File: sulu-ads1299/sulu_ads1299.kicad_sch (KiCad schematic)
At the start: 27 parts, among them J1 Conn_02x11_Odd_Even, J2 Conn_02x10_Odd_Even, J3 Conn_01x10, J4 Conn_02x07_Odd_Even, J5 73391-0060, J6 Conn_01x02, SW1 SW_Push, U3 S-85S1AB18-I6T1U, U4 S-85S1AB11-I6T1U, U5 LM2775DSG

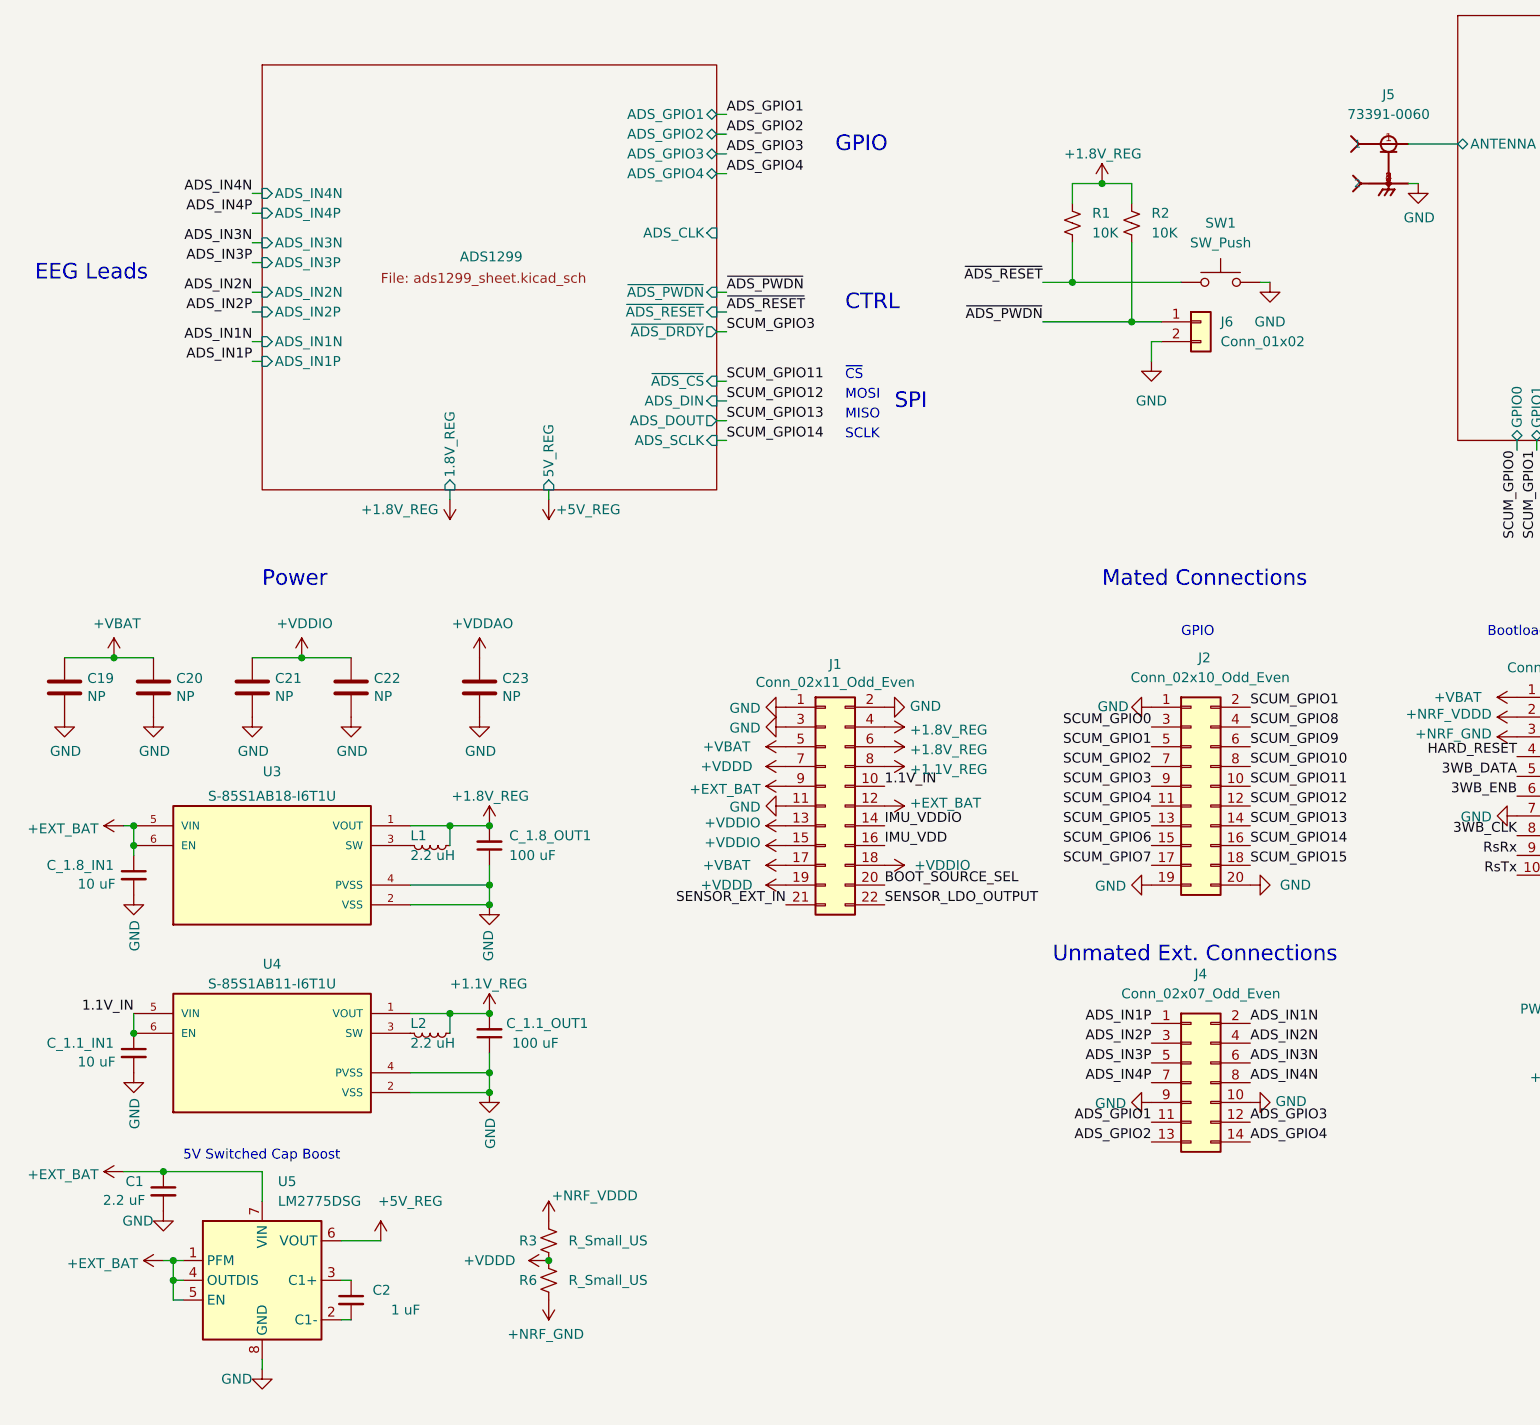
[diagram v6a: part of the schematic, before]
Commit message: Sulu-ads1299, completed place & route
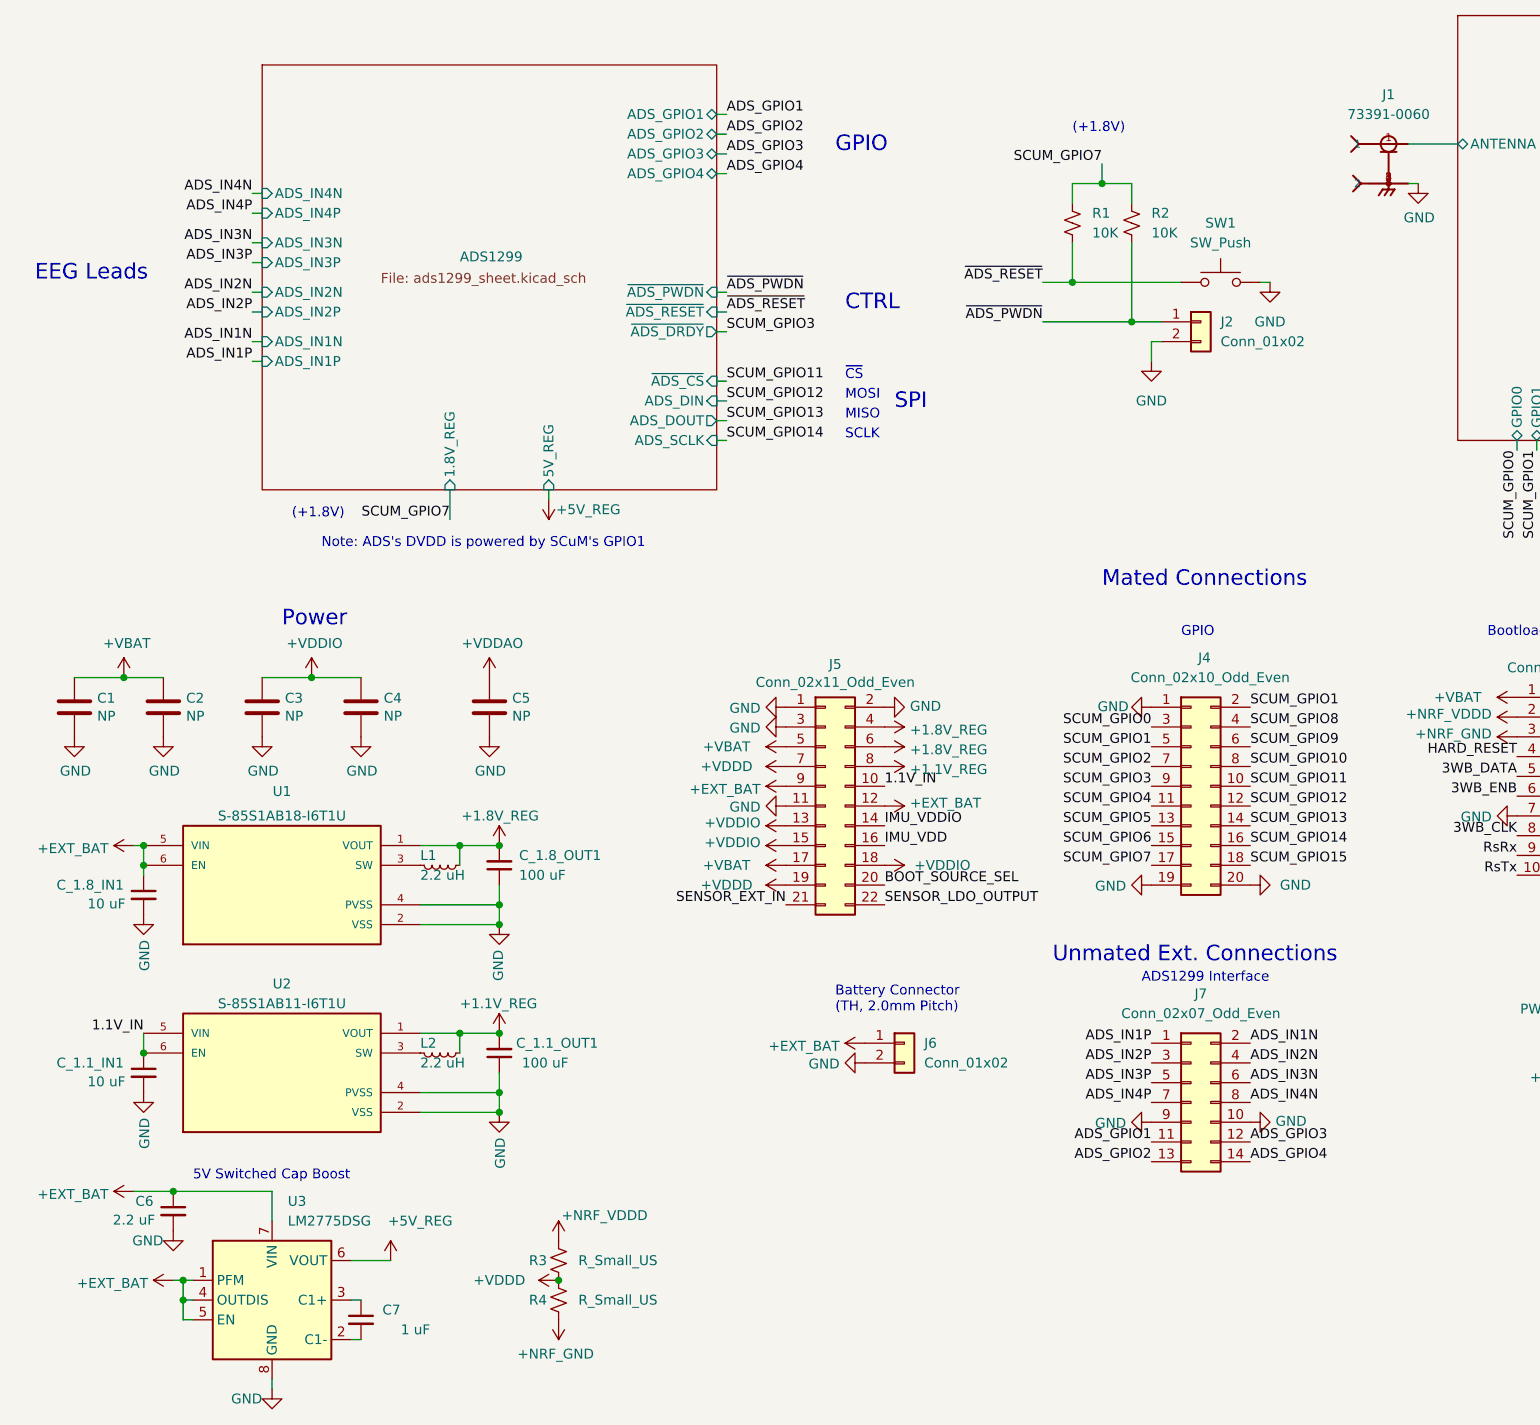
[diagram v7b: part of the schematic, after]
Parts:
- added J6: Conn_01x02, Connector_JST:JST_PH_B2B-PH-K_1x02_P2.00mm_Vertical, symbol Connector_Generic:Conn_01x02
- SW1: footprint (none) -> Button_Switch_THT:SW_PUSH_6mm
- renumbered C19 to C1, C20 to C2, C21 to C3, C22 to C4, C23 to C5, C1 to C6, C2 to C7, J5 to J1, J6 to J2, J2 to J4, J1 to J5, J4 to J7, R6 to R4, U3 to U1, U4 to U2, U5 to U3
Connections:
- net +1.8V_REG: no longer R1.1, R2.1
- net +EXT_BAT: now also J6.1 (Pin_1)
- net GND: now also J6.2 (Pin_2)
- net SCUM_GPIO7: now also R1.1, R2.1
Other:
- sheet ADS1299 ports: added none; removed ADS_CLK
- note added: "(+1.8V)"
- note added: "ADS1299 Interface"
- note added: "Battery Connector (TH, 2.0mm Pitch)"
- note added: "Note: ADS's DVDD is powered by SCuM's GPIO1"
- moved on the sheet: C1, C2, C3, C4, C5, C6, C7, C_1.1_IN1, C_1.1_OUT1, C_1.8_IN1, C_1.8_OUT1, J7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

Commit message: Sulu-ads1299 switched to backside female connectors
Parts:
- J3: footprint Connector_PinHeader_2.54mm:PinHeader_1x10_P2.54mm_Vertical -> Connector_PinSocket_2.54mm:PinSocket_1x10_P2.54mm_Vertical
- J4: footprint Connector_PinHeader_2.54mm:PinHeader_2x10_P2.54mm_Vertical -> Connector_PinSocket_2.54mm:PinSocket_2x10_P2.54mm_Vertical
- J5: footprint Connector_PinHeader_2.54mm:PinHeader_2x11_P2.54mm_Vertical -> Connector_PinSocket_2.54mm:PinSocket_2x11_P2.54mm_Vertical
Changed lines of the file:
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@@
       (effects (font (size 1.27 1.27)) (justify left))
     )
-    (property "Footprint" "Connector_PinHeader_2.54mm:PinHeader_1x10_P2.54mm_Vertical" (id 2) (at 209.55 116.84 0)
+    (property "Footprint" "Connector_PinSocket_2.54mm:PinSocket_1x10_P2.54mm_Vertical" (id 2) (at 209.55 116.84 0)
       (effects (font (size 1.27 1.27)) hide)
     )
@@
     (property "Reference" "J5" (id 0) (at 116.84 102.4382 0))
     (property "Value" "Conn_02x11_Odd_Even" (id 1) (at 116.84 104.7496 0))
-    (property "Footprint" "Connector_PinHeader_2.54mm:PinHeader_2x11_P2.54mm_Vertical" (id 2) (at 115.57 120.65 0)
+    (property "Footprint" "Connector_PinSocket_2.54mm:PinSocket_2x11_P2.54mm_Vertical" (id 2) (at 115.57 120.65 0)
       (effects (font (size 1.27 1.27)) hide)
     )
@@
       (effects (font (size 1.27 1.27)) (justify right))
     )
-    (property "Footprint" "Connector_PinHeader_2.54mm:PinHeader_2x10_P2.54mm_Vertical" (id 2) (at 162.56 118.11 0)
+    (property "Footprint" "Connector_PinSocket_2.54mm:PinSocket_2x10_P2.54mm_Vertical" (id 2) (at 162.56 118.11 0)
       (effects (font (size 1.27 1.27)) hide)
     )
@@
     )
     (path "/06d263f3-9a94-4d17-b8dd-31a84d0f68d4"
-      (reference "J3") (unit 1) (value "Conn_01x10") (footprint "Connector_PinHeader_2.54mm:PinHeader_1x10_P2.54mm_Vertical")
+      (reference "J3") (unit 1) (value "Conn_01x10") (footprint "Connector_PinSocket_2.54mm:PinSocket_1x10_P2.54mm_Vertical")
     )
     (path "/7a11f75a-d1cf-42d7-ac2f-6466370de990"
-      (reference "J4") (unit 1) (value "Conn_02x10_Odd_Even") (footprint "Connector_PinHeader_2.54mm:PinHeader_2x10_P2.54mm_Vertical")
+      (reference "J4") (unit 1) (value "Conn_02x10_Odd_Even") (footprint "Connector_PinSocket_2.54mm:PinSocket_2x10_P2.54mm_Vertical")
     )
     (path "/43b93f7b-5da3-420b-88a5-8fe6df4882cc"
-      (reference "J5") (unit 1) (value "Conn_02x11_Odd_Even") (footprint "Connector_PinHeader_2.54mm:PinHeader_2x11_P2.54mm_Vertical")
+      (reference "J5") (unit 1) (value "Conn_02x11_Odd_Even") (footprint "Connector_PinSocket_2.54mm:PinSocket_2x11_P2.54mm_Vertical")
     )
     (path "/40ce4037-dfe6-415e-bce1-84fa39ce46b1"
